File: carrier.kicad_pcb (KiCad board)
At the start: 4 copper layers, 20.3 x 68.6 mm, 66 parts, among them J1 Conn_02x06_Odd_Even, J10 Conn_01x02, J11 Conn_01x02, J12 AudioJack3_SwitchTR, J13 Conn_02x06_Odd_Even, J2 Conn_01x26, J3 Conn_01x26, J4 TYPE-C-31-M-12, J5 Conn_01x02, J6 Conn_01x02, J7 Conn_01x02, J8 Conn_01x02, J9 Conn_01x02, SW1 SW_Push, SW2 SW_Push, SW3 SW_Push, SW4 SW_Push, SW5 SW_Push, SW6 SW_Push, U1 CARAVEL, U2 W25Q128JVS, U3 LP5907MFX-3.3, U4 LP5907MFX-1.8, U5 LP5907MFX-1.8, U6 LP5907MFX-3.3, U7 TPD2E001DRSR, U8 OPA340NA, U9 OPA340NA, X1 SG-5032CAN

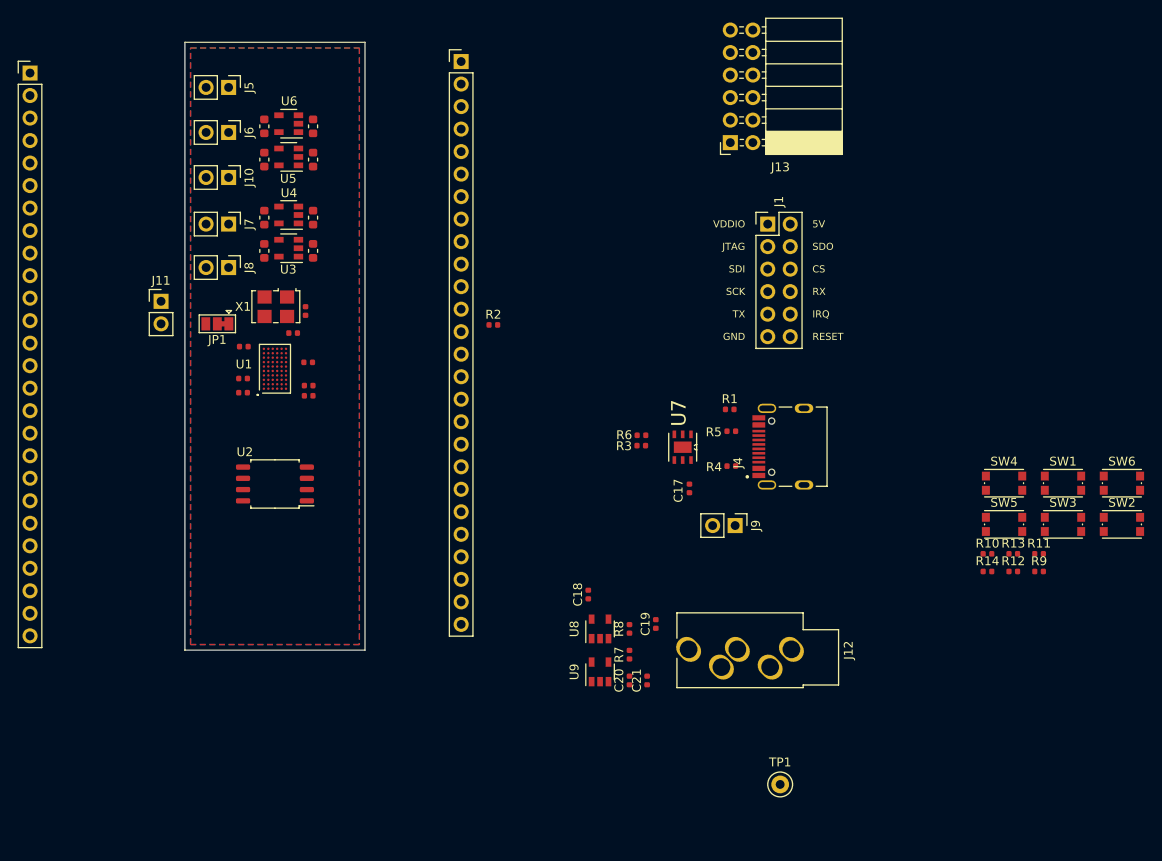
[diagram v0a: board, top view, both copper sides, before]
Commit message: Switch KiCAD standard SOT-23-5 footprint
No need to reinvent the wheel.
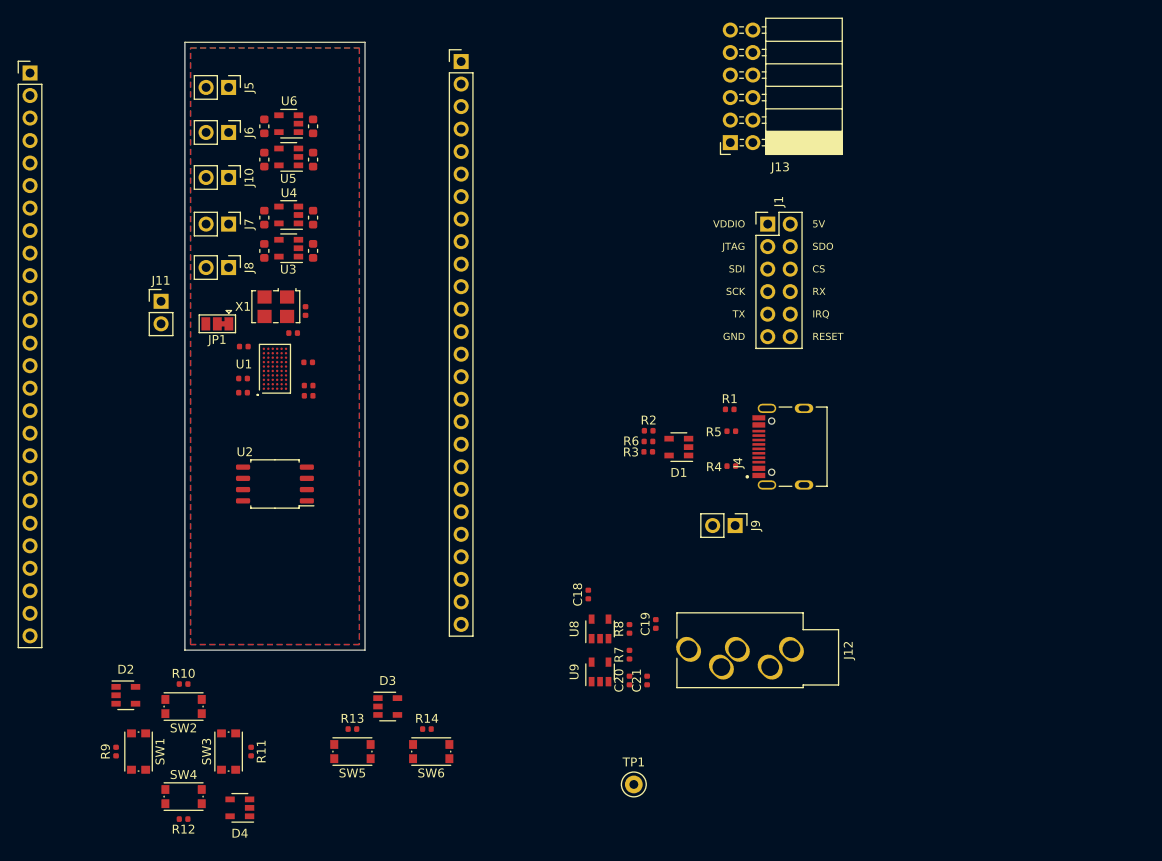
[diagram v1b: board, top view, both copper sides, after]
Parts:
- removed C17: 22n, Capacitor_SMD:C_0402_1005Metric
- removed U7: TPD2E001DRSR, TPD2E001DRSR:SON95P315X315X80-7N
- added D1: ESDS312DBVR, Package_TO_SOT_SMD:SOT-23-5, F.Cu at (114.3, 88.8)
- added D2: ESDS312DBVR, Package_TO_SOT_SMD:SOT-23-5, F.Cu at (51.9, 116.8)
- added D3: ESDS312DBVR, Package_TO_SOT_SMD:SOT-23-5, F.Cu at (81.5, 118.1)
- added D4: ESDS312DBVR, Package_TO_SOT_SMD:SOT-23-5, F.Cu at (64.8, 129.5)
- moved SW1 108.6 mm to (53.3, 123.2), turned to -90 degrees
- moved SW2 107.8 mm to (58.4, 118.1), turned to 180 degrees
- moved R9 106.1 mm to (50.8, 123.2), turned to 90 degrees
- moved SW4 99.1 mm to (58.4, 128.3)
- moved R12 97.7 mm to (58.4, 130.8), turned to 180 degrees
- moved SW3 97.6 mm to (63.5, 123.2), turned to 90 degrees
- moved R10 91.9 mm to (58.4, 115.6)
- moved R11 91.7 mm to (66.0, 123.2), turned to -90 degrees
- moved SW6 83.6 mm to (86.4, 123.2), turned to 180 degrees
- moved SW5 77.9 mm to (77.5, 123.2), turned to 180 degrees
- moved R13 77.1 mm to (77.5, 120.7)
- moved R14 65.7 mm to (85.9, 120.7)
- moved R2 21.2 mm to (110.9, 87.0)
- moved TP1 16.5 mm to (109.2, 126.9)
- moved R3 1.05 mm to (110.8, 89.4)
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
